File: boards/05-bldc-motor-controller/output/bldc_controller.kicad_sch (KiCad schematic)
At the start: 51 parts, among them J1 Power Input, J2 Motor Output, J3 Hall Sensors, J4 SWD-6, Q1 IRLZ44N, Q2 IRLZ44N, Q3 IRLZ44N, Q4 IRLZ44N, Q5 IRLZ44N, Q6 IRLZ44N, U1 LM2596-5.0, U10 STM32G431K8Tx, U2 AMS1117-3.3, U3 DRV8301, Y1 8MHz

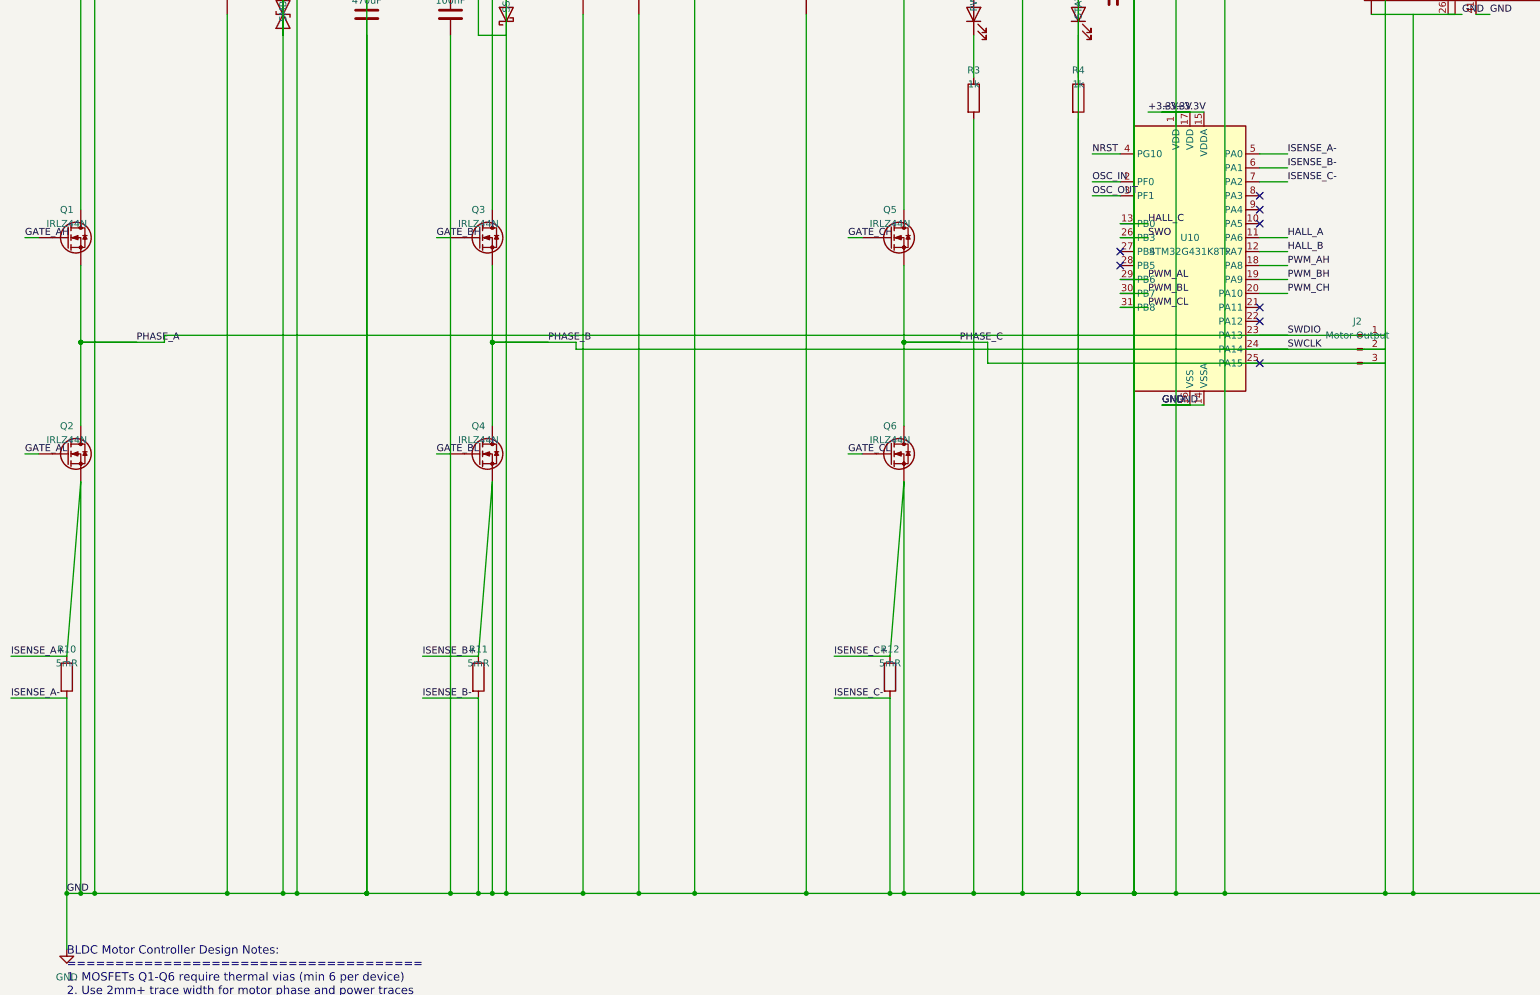
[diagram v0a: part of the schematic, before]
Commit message: fix(boards/05): U10 SWDIO/SWCLK/ISENSE wire-stub collision in _connect_mcu_pin_to_label (#3382)
Closes #3379

PR #3377 fixed the kicad-cli ``/``-prefix strip and unconditional pin-to-pad
map in ``kct pcb sync-netlist`` but deliberately did not refresh the
committed routed PCB because applying that sync exposed a *separate*
defect in ``boards/05-bldc-motor-controller/design.py``:
``_connect_mcu_pin_to_label`` placed each U10 stub-and-label without
checking whether the label coordinate landed on the interior of a
foreign wire.

Three categories of silent net-bridging resulted, all surfaced by
kicad-cli:

* ``U10.23`` (SWDIO) -> ``/PHASE_A`` (sat on the long horizontal wire
  from J2 west to HB_A's VOUT).
* ``U10.24`` (SWCLK) -> ``/PHASE_B`` (same mechanism, HB_B row).
* ``U10.14`` / ``16`` / ``32`` (GND) -> ``+3V3`` (the leftward GND
  stub at x=227.33 sat on a vertical HallSensorInput rail that also
  passed through the ``+3.3V`` label row at y=137.16).
* ``U10.5`` / ``6`` / ``7`` (ISENSE_A-/B-/C-) -> ``+3V3`` (same
  x=227.33 vertical-rail bridge through the ISENSE label row).

Applying ``kct pcb sync-netlist`` with those bridges in place
rewrote U10's pad nets to match the schematic and regressed DRC
from 6 to 73 violations, breaking the #3258 hot-spot invariant.

Fix:

* ``_connect_mcu_pin_to_label`` is now collision-aware. Mirroring the
  ``_emit_pin_net_stub`` helper in ``schematic/blocks/_stub_helpers.py``,
  it tries the requested geometry first, then escalates through
  progressively longer horizontal stubs in the same direction, a
  vertical nudge, the opposite-side stub, and finally L-shaped routes
  (horizontal+vertical to a free row). Snapped candidate coordinates
  are checked against ``_stub_endpoint_would_collide``; the first
  collision-free candidate wins. A ``ValueError`` is raised when no
  candidate clears -- silent net-bridging is unrecoverable at
  netlist time.
* All 24 U10 pin labels are *deferred* to after Section 11 (design
  notes). Without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
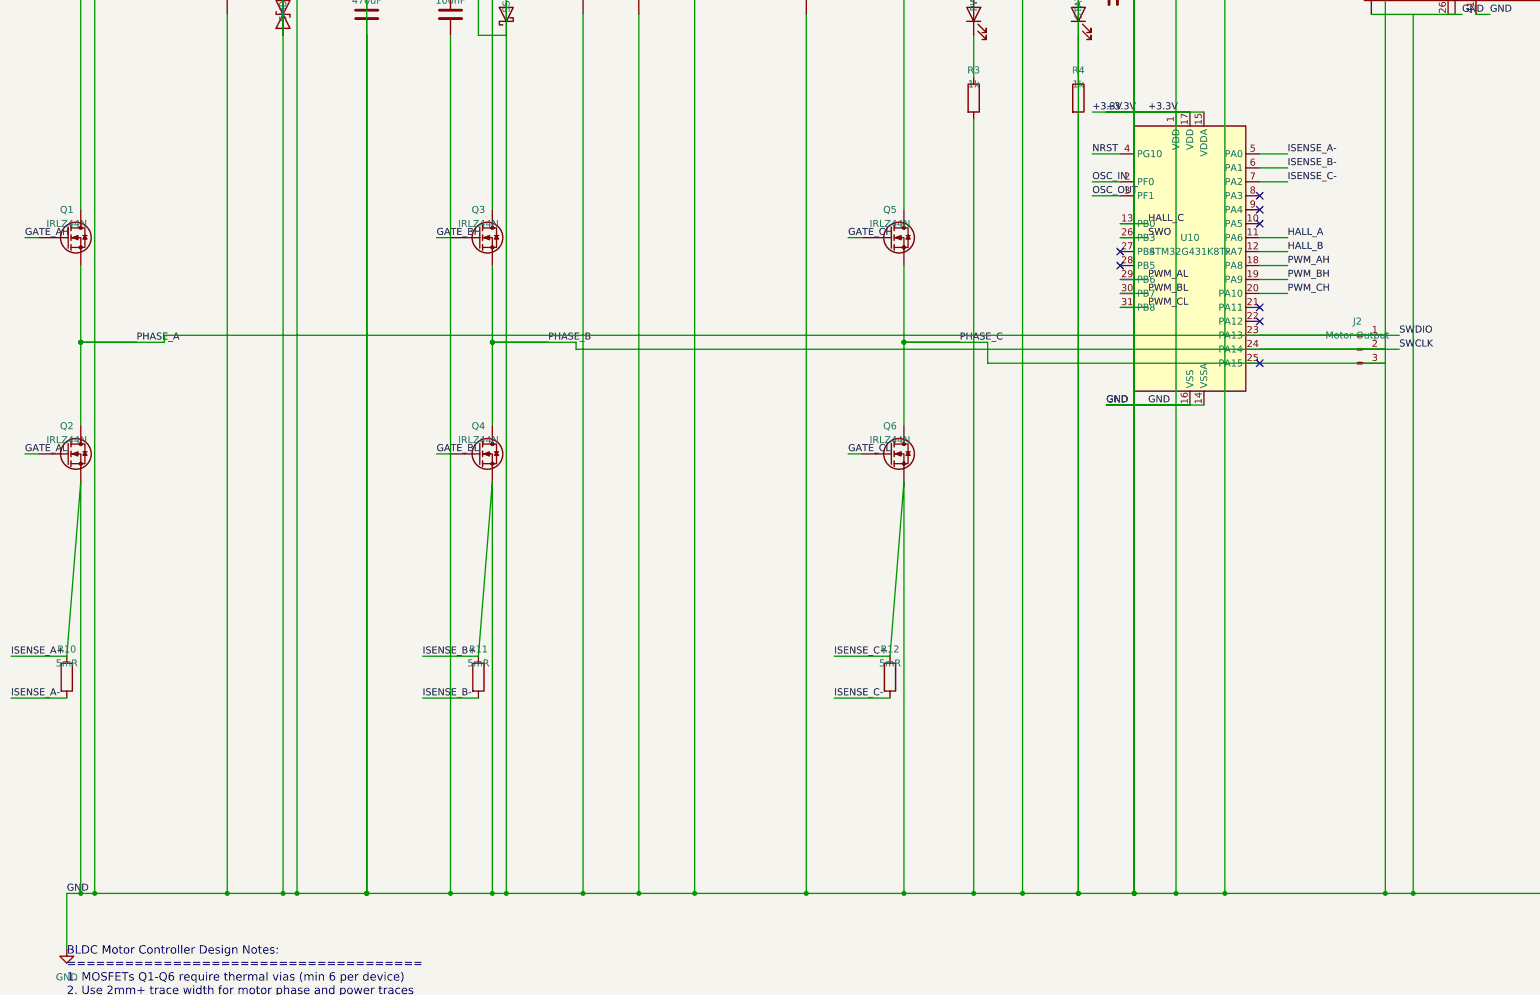
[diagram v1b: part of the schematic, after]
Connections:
- net +24V: no longer R10.2, R11.2, R12.2, U10.5 (PA0), U10.6 (PA1), U10.7 (PA2)
- new net ISENSE_A-: R10.2, U10.5 (PA0)
- new net ISENSE_B-: R11.2, U10.6 (PA1)
- new net ISENSE_C-: R12.2, U10.7 (PA2)

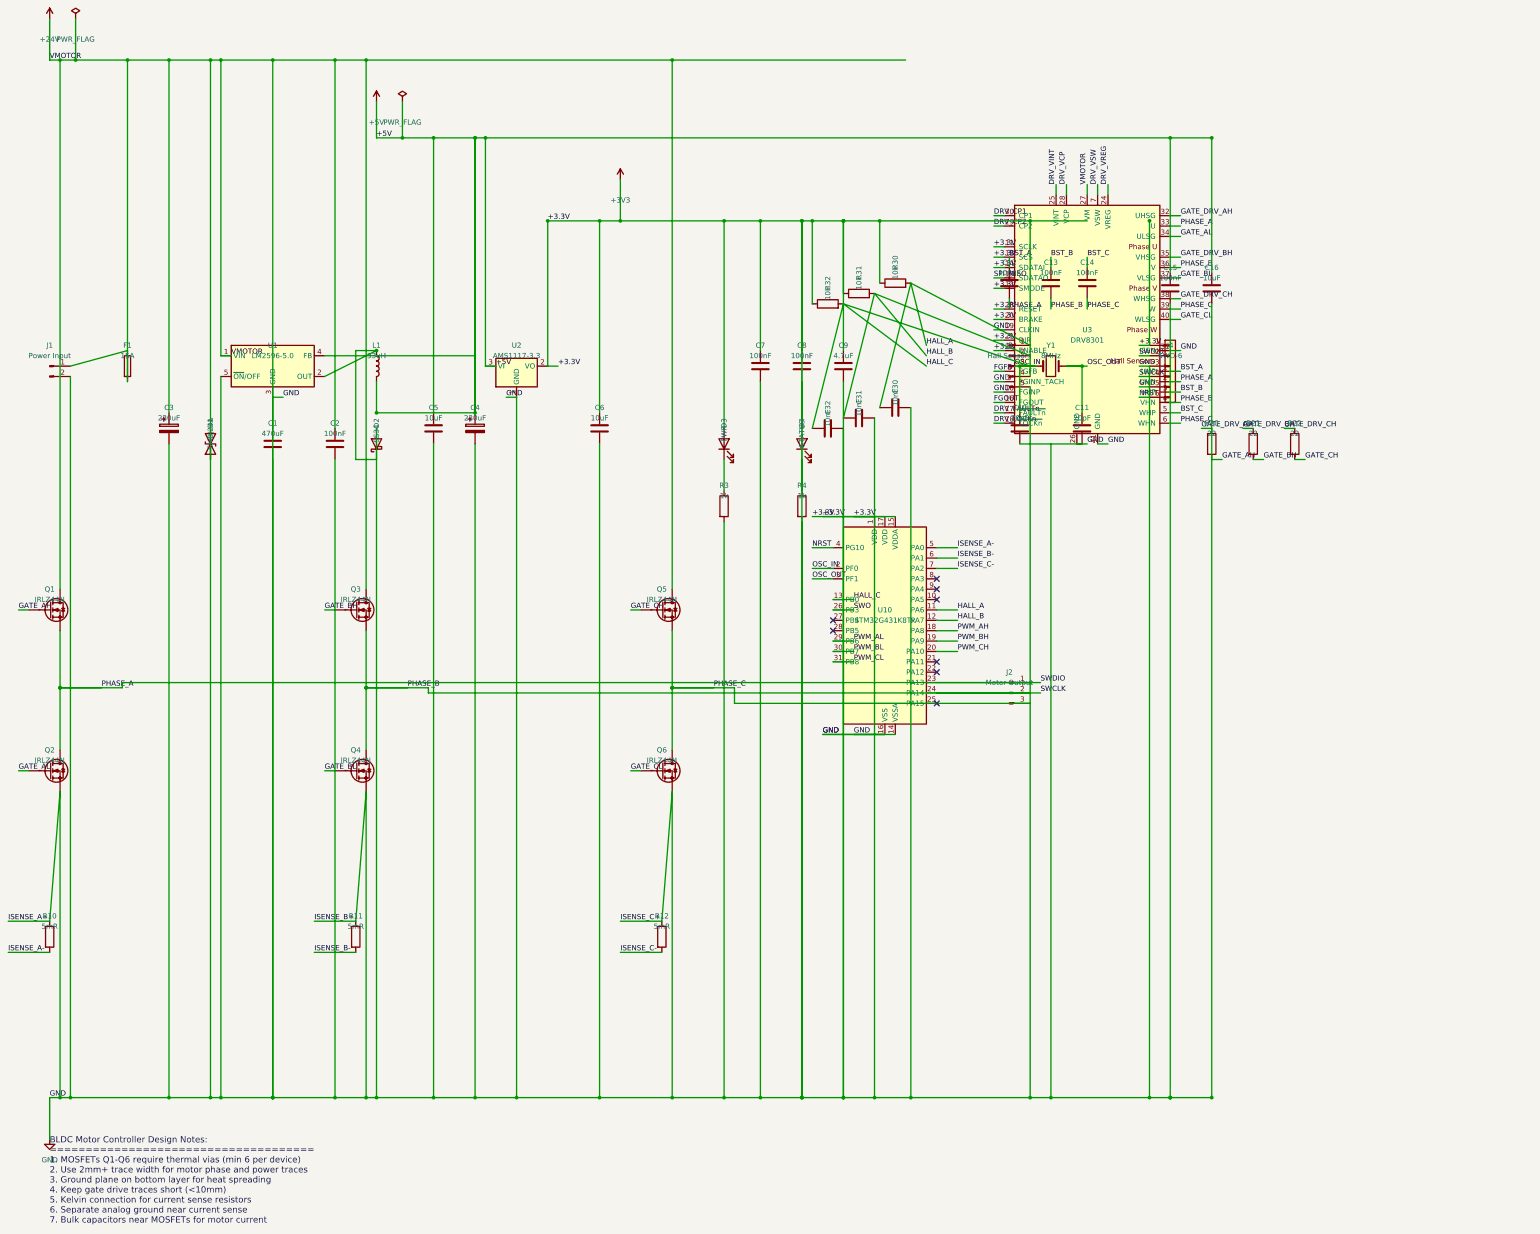
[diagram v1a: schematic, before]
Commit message: fix(boards/05): full U3 DRV8301 schematic symbol swap with layout refactor
Issue #3384 (PR #3388) reconciled the BOM/PCB/schematic-value triangle
around U3 and shipped the project-local board05_custom:DRV8301 symbol
library (57-pin HTSSOP-56), but deferred the schematic-side swap because
naïvely placing the new symbol at the historical X_GATE_DRV=280
silently bridged AGND (pin 28) to +3.3V via a J3 Hall-connector column
wire that ran through the DRV8301 left-edge pin lines at x=265.43.

This PR completes the swap:

* design.py now registers the project-local symbol library via the
  Schematic(local_symbol_libs=[...]) param and places U3 directly via
  add_symbol("board05_custom:DRV8301", ...), bypassing GateDriverBlock
  (which hard-codes Driver_Motor:DRV8308).  U3's bootstrap caps
  (C12-C14) and bypass caps (C15-C16) are now created via the existing
  factory helpers + Device:C symbols rather than as block side-effects.

* U3 is placed at (355, 145) -- well east of J3's column wires at
  x=265.43 (the original AGND-vs-+3.3V short) AND clear of R22's
  output stub at (332.74, 123.19) (the secondary GND-vs-GATE_CH
  short that would have hit if U3 sat at x=350).

* All 57 DRV8301 pins now emit per-pin stub wires + labels via
  _emit_pin_net_stub for pins 1-56 and a manual vertical stub for
  pin 57 (PowerPAD, GND).  Net mapping mirrors DRV8301_PINS in the
  PCB-side block.

* Replaces tests/test_board_05_drv8308_pin_nets.py with
  tests/test_board_05_drv8301_pin_nets.py, holding the
  DRV8301-symbol shape, label-on-wire invariant, and the
  AGND-must-be-GND / PWRGD-must-be-+3.3V anti-regression assertion.

Sync-netlist drift on U3: 41 (DRV8308 schematic) -> 19 (this PR).
The 19 remaining U3 mismatches are pure rail-name normalizations
("+3.3V" -> "+3V3", "VMOTOR" -> "+24V") that affect every component
on those rails (J3.4, J4.1, U10.1, etc.) -- a separate global
schematic vs power-symbol naming concern, NOT a U3 pinout error.

ERC: 17 -> 16 violations (1 new lib_sym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
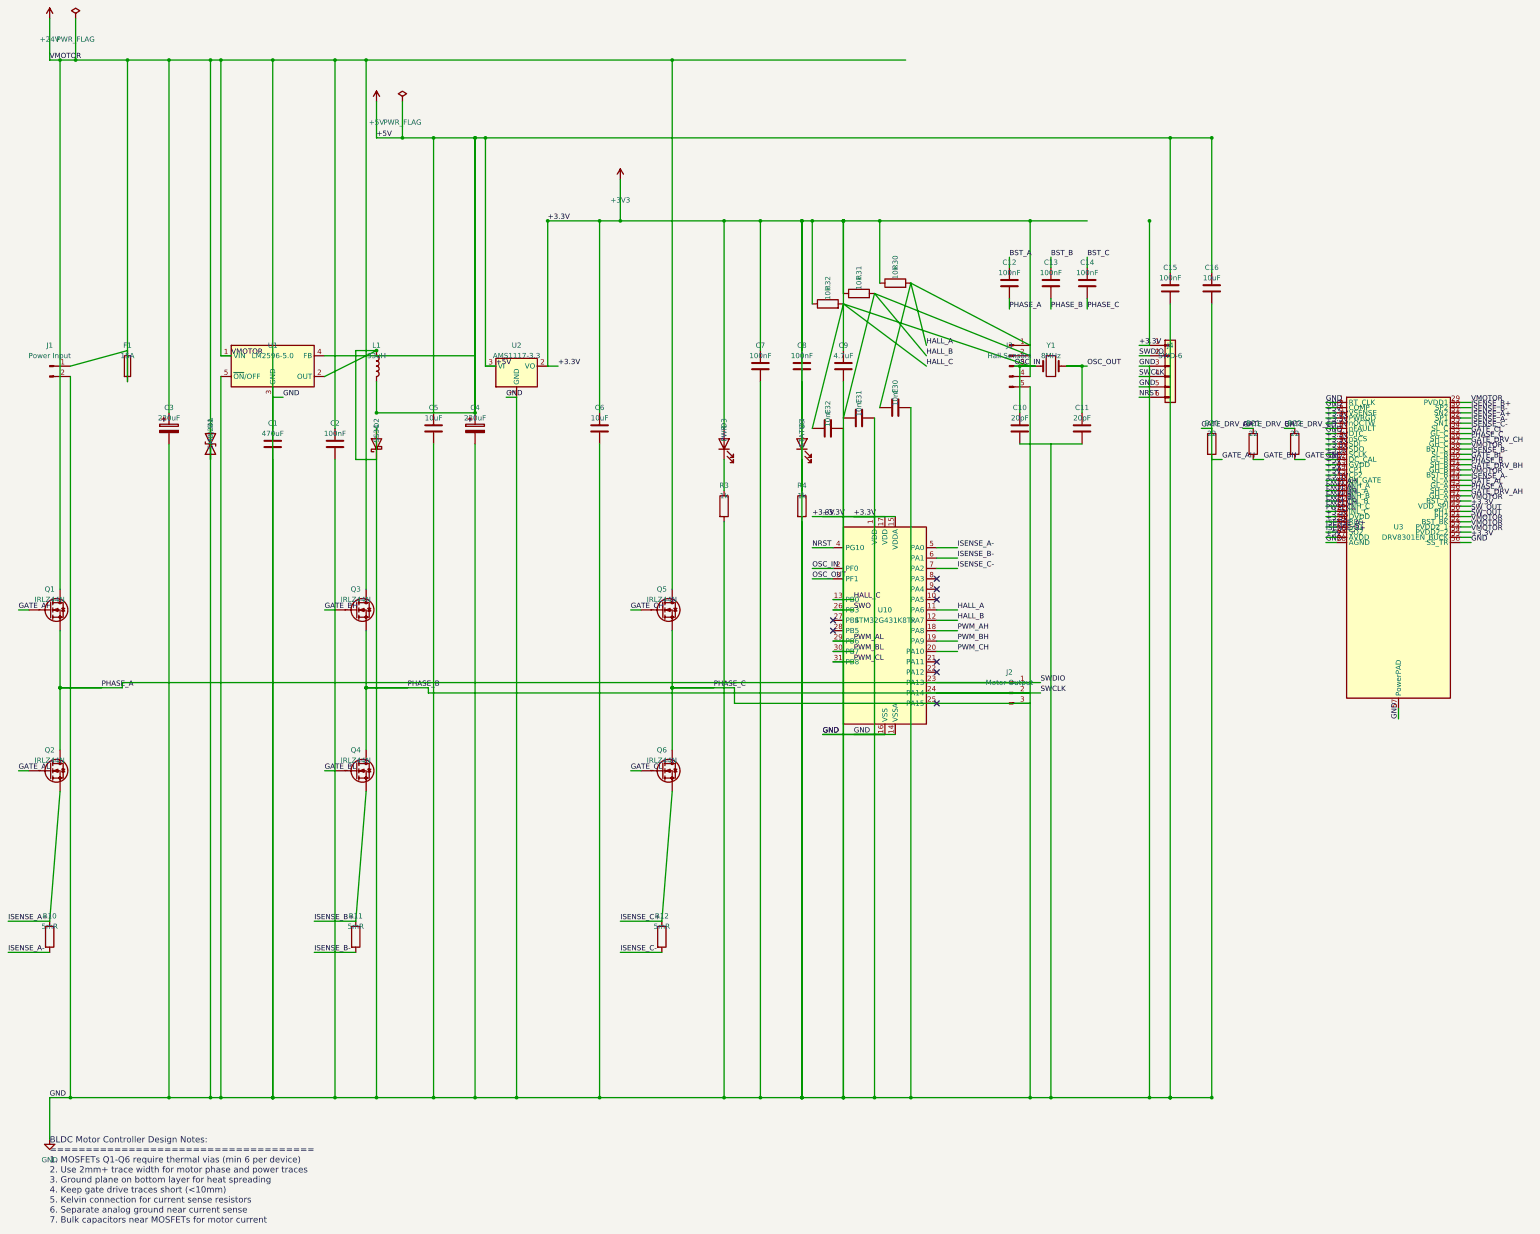
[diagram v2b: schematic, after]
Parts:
- removed U3: DRV8301, symbol Driver_Motor:DRV8308
- added U3: DRV8301, Package_SO:HTSSOP-56-1EP_6.1x14mm_P0.5mm_EP3.61x6.35mm, symbol board05_custom:DRV8301
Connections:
- net +24V: now also U3.1 (RT_CLK), U3.10 (SDO), U3.11 (SCLK), U3.12 (DC_CAL), U3.16 (EN_GATE), U3.2 (COMP), U3.23 (DVDD), U3.24 (REF), U3.28 (AGND), U3.29 (PVDD1), U3.38 (BST_C), U3.4 (PWRGD), U3.43 (BST_B), U3.48 (BST_A), U3.49 (VDD_SPI), U3.5 (nOCTW), U3.52 (BST_BK), U3.53 (PVDD2_1), U3.54 (PVDD2_2), U3.55 (EN_BUCK), U3.56 (SS_TR), U3.57 (PowerPAD), U3.6 (nFAULT), U3.7 (DTC), U3.8 (nSCS), U3.9 (SDI); no longer C10.2, C11.2, Q2.S, Q4.S, Q6.S, R10.1, R11.1, R12.1
- net +5V: now also U3.13 (GVDD), U3.14 (CP1), U3.15 (CP2), U3.27 (AVDD), U3.3 (VSENSE)
- net GATE_AL: now also U3.45 (GL_A)
- net GATE_BL: now also U3.40 (GL_B)
- net GATE_CL: now also U3.35 (GL_C)
- net GATE_DRV_AH: now also U3.47 (GH_A)
- net GATE_DRV_BH: now also U3.42 (GH_B)
- net GATE_DRV_CH: now also U3.37 (GH_C)
- net ISENSE_A-: now also U3.33 (SN1), U3.44 (SL_A)
- net ISENSE_B-: now also U3.31 (SN2), U3.39 (SL_B)
- net ISENSE_C-: now also U3.34 (SL_C)
- net PHASE_A: now also U3.46 (SH_A)
- net PHASE_B: now also U3.41 (SH_B)
- net PHASE_C: now also U3.36 (SH_C)
- net PWM_AH: now also U3.17 (INH_A)
- net PWM_AL: now also U3.18 (INL_A)
- net PWM_BH: now also U3.19 (INH_B)
- net PWM_BL: now also U3.20 (INL_B)
- net PWM_CH: now also U3.21 (INH_C)
- net PWM_CL: now also U3.22 (INL_C)
- new net: C10.2, C11.2
- new net ISENSE_A+: Q2.S, R10.1, U3.25 (SO1), U3.32 (SP1)
- new net ISENSE_B+: Q4.S, R11.1, U3.26 (SO2), U3.30 (SP2)
- new net ISENSE_C+: Q6.S, R12.1
- new net SW_OUT: U3.50 (PH1), U3.51 (PH2)
